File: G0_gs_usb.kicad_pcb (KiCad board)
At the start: 2 copper layers, 25.9 x 53.3 mm, 59 parts, among them J1 USB_C_Receptacle_USB2.0, J2 CAN1, J3 CAN2, J4 Conn_01x03_Pin, SW1 SW_Push_Dual, U1 STM32G0B1CBTx, U2 TJA1042T-3, U3 TJA1042T-3, U4 XC6206PxxxMR

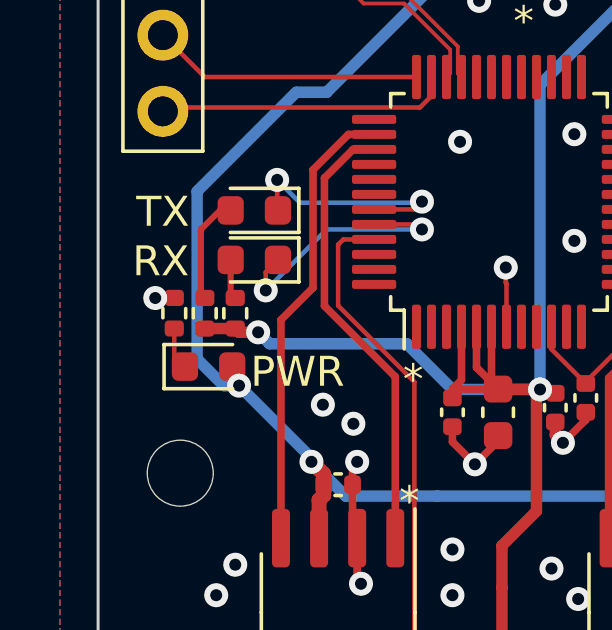
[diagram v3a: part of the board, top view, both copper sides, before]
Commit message: Update net labels to match the purpose of the pins.
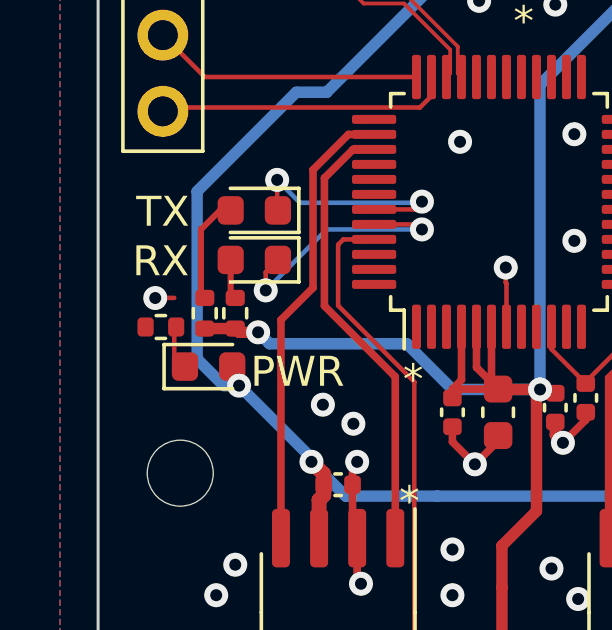
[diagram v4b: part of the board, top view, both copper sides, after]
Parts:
- R10, R11, R12, R13: value 22 -> 1k
- R14: value 1k -> 5.1k
- moved R14 0.64 mm to (54.2, 88.3), turned to 0 degrees
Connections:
- R14 pad 1: Net-(D8-K) -> GND
- R14 pad 2: GND -> Net-(D8-K)
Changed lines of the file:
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@@
+    )
+  )
+  (footprint "Resistor_SMD:R_0402_1005Metric" (layer "F.Cu")
+    (at 54.162939 88.342353)
+    (descr "Resistor SMD 0402 (1005 Metric), square (rectangular) end terminal, IPC_7351 nominal, (Body size source: IPC-SM-782 page 72, https://www.pcb-3d.com/wordpress/wp-content/uploads/ipc-sm-782a_amendment_1_and_2.pdf), generated with kicad-footprint-generator")
+    (tags "resistor")
+    (property "LCSC Part #" "C11616")
+    (property "Part #" "0402WGF5103TCE")
+    (property "Sheetfile" "G0_gs_usb.kicad_sch")
+    (property "Sheetname" "")
+    (property "ki_description" "Resistor")
+    (property "ki_keywords" "R res resistor")
+    (attr smd)
+    (fp_text reference "R14" (at 0 -1.17) (layer "F.SilkS") hide
+        (effects (font (size 1 1) (thickness 0.15)))
+    )
+    (fp_text value "5.1k" (at 0 1.17) (layer "F.Fab")
+        (effects (font (size 1 1) (thickness 0.15)))
+    )
+    (fp_text user "${REFERENCE}" (at 0 0) (layer "F.Fab")
+        (effects (font (size 0.26 0.26) (thickness 0.04)))
+    )
+    (fp_line (start -0.153641 -0.38) (end 0.153641 -0.38)
+      (stroke (width 0.12) (type solid)) (layer "F.SilkS"))
+    (fp_line (start -0.153641 0.38) (end 0.153641 0.38)
+      (stroke (width 0.12) (type solid)) (layer "F.SilkS"))
+    (fp_line (start -0.93 -0.47) (end 0.93 -0.47)
+      (stroke (width 0.05) (type solid)) (layer "F.CrtYd"))
+    (fp_line (start -0.93 0.47) (end -0.93 -0.47)
+      (stroke (width 0.05) (type solid)) (layer "F.CrtYd"))
+    (fp_line (start 0.93 -0.47) (end 0.93 0.47)
+      (stroke (width 0.05) (type solid)) (layer "F.CrtYd"))
+    (fp_line (start 0.93 0.47) (end -0.93 0.47)
+      (stroke (width 0.05) (type solid)) (layer "F.CrtYd"))
+    (fp_line (start -0.525 -0.27) (end 0.525 -0.27)
+      (stroke (width 0.1) (type solid)) (layer "F.Fab"))
+    (fp_line (start -0.525 0.27) (end -0.525 -0.27)
+      (stroke (width 0.1) (type solid)) (layer "F.Fab"))
+    (fp_line (start 0.525 -0.27) (end 0.525 0.27)
+      (stroke (width 0.1) (type solid)) (layer "F.Fab"))
+    (fp_line (start 0.525 0.27) (end -0.525 0.27)
+      (stroke (width 0.1) (type solid)) (layer "F.Fab"))
+    (pad "1" smd roundrect (at -0.51 0) (size 0.54 0.64) (layers "F.Cu" "F.Paste" "F.Mask") (roundrect_rratio 0.25)
+      (net 2 "GND") (pintype "passive"))
+    (pad "2" smd roundrect (at 0.51 0) (size 0.54 0.64) (layers "F.Cu" "F.Paste" "F.Mask") (roundrect_rratio 0.25)
+      (net 9 "Net-(D8-K)") (pintype "passive"))
+    (model "${KICAD6_3DMODEL_DIR}/Resistor_SMD.3dshapes/R_0402_1005Metric.wrl"
+      (offset (xyz 0 0 0))
+      (scale (xyz 1 1 1))
+      (rotate (xyz 0 0 0))
     )
   )
@@
     (descr "Resistor SMD 0402 (1005 Metric), square (rectangular) end terminal, IPC_7351 nominal, (Body size source: IPC-SM-782 page 72, https://www.pcb-3d.com/wordpress/wp-content/uploads/ipc-sm-782a_amendment_1_and_2.pdf), generated with kicad-footprint-generator")
     (tags "resistor")
-    (property "LCSC Part #" "C25092")
-    (property "Part #" "0402WGF220JTCE")
+    (property "LCSC Part #" "C11702")
+    (property "Part #" "0402WGF1001TCE")
     (property "Sheetfile" "G0_gs_usb.kicad_sch")
     (property "Sheetname" "")
@@
         (effects (font (size 1 1) (thickness 0.15)))
     )
-    (fp_text value "22" (at 0 1.17 -90) (layer "F.Fab")
+    (fp_text value "1k" (at 0 1.17 -90) (layer "F.Fab")
         (effects (font (size 1 1) (thickness 0.15)))
     )
@@
       (net 4 "/5V") (pinfunction "A") (pintype "passive"))
     (model "${KICAD6_3DMODEL_DIR}/LED_SMD.3dshapes/LED_0603_1608Metric.wrl"
-      (offset (xyz 0 0 0))
-      (scale (xyz 1 1 1))
-      (rotate (xyz 0 0 0))
-    )
-  )
-  (footprint "Resistor_SMD:R_0402_1005Metric" (layer "F.Cu")
-    (at 54.61 87.882 90)
-    (descr "Resistor SMD 0402 (1005 Metric), square (rectangular) end terminal, IPC_7351 nominal, (Body size source: IPC-SM-782 page 72, https://www.pcb-3d.com/wordpress/wp-content/uploads/ipc-sm-782a_amendment_1_and_2.pdf), generated with kicad-footprint-generator")
-    (tags "resistor")
-    (property "LCSC Part #" "C11702")
-    (property "Part #" "0402WGF1001TCE")
-    (property "Sheetfile" "G0_gs_usb.kicad_sch")
-    (property "Sheetname" "")
-    (property "ki_description" "Resistor")
-    (property "ki_keywords" "R res resistor")
-    (attr smd)
-    (fp_text reference "R14" (at 0 -1.17 90) (layer "F.SilkS") hide
-        (effects (font (size 1 1) (thickness 0.15)))
-    )
-    (fp_text value "1k" (at 0 1.17 90) (layer "F.Fab")
-        (effects (font (size 1 1) (thickness 0.15)))
-    )
-    (fp_text user "${REFERENCE}" (at 0 0 90) (layer "F.Fab")
-        (effects (font (size 0.26 0.26) (thickness 0.04)))
-    )
-    (fp_line (start -0.153641 -0.38) (end 0.153641 -0.38)
-      (stroke (width 0.12) (type solid)) (layer "F.SilkS"))
-    (fp_line (start -0.153641 0.38) (end 0.153641 0.38)
-      (stroke (width 0.12) (type solid)) (layer "F.SilkS"))
-    (fp_line (start -0.93 -0.47) (end 0.93 -0.47)
-      (stroke (width 0.05) (type solid)) (layer "F.CrtYd"))
-    (fp_line (start -0.93 0.47) (end -0.93 -0.47)
-      (stroke (width 0.05) (type solid)) (layer "F.CrtYd"))
-    (fp_line (start 0.93 -0.47) (end 0.93 0.47)
-      (stroke (width 0.05) (type solid)) (layer "F.CrtYd"))
-    (fp_line (start 0.93 0.47) (end -0.93 0.47)
-      (stroke (width 0.05) (type solid)) (layer "F.CrtYd"))
-    (fp_line (start -0.525 -0.27) (end 0.525 -0.27)
-      (stroke (width 0.1) (type solid)) (layer "F.Fab"))
-    (fp_line (start -0.525 0.27) (end -0.525 -0.27)
-      (stroke (width 0.1) (type solid)) (layer "F.Fab"))
-    (fp_line (start 0.525 -0.27) (end 0.525 0.27)
-      (stroke (width 0.1) (type solid)) (layer "F.Fab"))
-    (fp_line (start 0.525 0.27) (end -0.525 0.27)
-      (stroke (width 0.1) (type solid)) (layer "F.Fab"))
-    (pad "1" smd roundrect (at -0.51 0 90) (size 0.54 0.64) (layers "F.Cu" "F.Paste" "F.Mask") (roundrect_rratio 0.25)
-      (net 9 "Net-(D8-K)") (pintype "passive"))
-    (pad "2" smd roundrect (at 0.51 0 90) (size 0.54 0.64) (layers "F.Cu" "F.Paste" "F.Mask") (roundrect_rratio 0.25)
-      (net 2 "GND") (pintype "passive"))
-    (model "${KICAD6_3DMODEL_DIR}/Resistor_SMD.3dshapes/R_0402_1005Metric.wrl"
       (offset (xyz 0 0 0))
       (scale (xyz 1 1 1))
@@
     (descr "Resistor SMD 0402 (1005 Metric), square (rectangular) end terminal, IPC_7351 nominal, (Body size source: IPC-SM-782 page 72, https://www.pcb-3d.com/wordpress/wp-content/uploads/ipc-sm-782a_amendment_1_and_2.pdf), generated with kicad-footprint-generator")
     (tags "resistor")
-    (property "LCSC Part #" "C25092")
-    (property "Part #" "0402WGF220JTCE")
+    (property "LCSC Part #" "C11702")
+    (property "Part #" "0402WGF1001TCE")
     (property "Sheetfile" "G0_gs_usb.kicad_sch")
     (property "Sheetname" "")
@@
         (effects (font (size 1 1) (thickness 0.15)))
     )
-    (fp_text value "22" (at 0 1.17 90) (layer "F.Fab")
+    (fp_text value "1k" (at 0 1.17 90) (layer "F.Fab")
         (effects (font (size 1 1) (thickness 0.15)))
     )
@@
     (descr "Resistor SMD 0402 (1005 Metric), square (rectangular) end terminal, IPC_7351 nominal, (Body size source: IPC-SM-782 page 72, https://www.pcb-3d.com/wordpress/wp-content/uploads/ipc-sm-782a_amendment_1_and_2.pdf), generated with kicad-footprint-generator")
     (tags "resistor")
-    (property "LCSC Part #" "C25092")
-    (property "Part #" "0402WGF220JTCE")
+    (property "LCSC Part #" "C11702")
+    (property "Part #" "0402WGF1001TCE")
     (property "Sheetfile" "G0_gs_usb.kicad_sch")
     (property "Sheetname" "")
@@
         (effects (font (size 1 1) (thickness 0.15)))
     )
-    (fp_text value "22" (at 0 1.17 -90) (layer "F.Fab")
+    (fp_text value "1k" (at 0 1.17 -90) (layer "F.Fab")
         (effects (font (size 1 1) (thickness 0.15)))
     )
@@
     (descr "Resistor SMD 0402 (1005 Metric), square (rectangular) end terminal, IPC_7351 nominal, (Body size source: IPC-SM-782 page 72, https://www.pcb-3d.com/wordpress/wp-content/uploads/ipc-sm-782a_amendment_1_and_2.pdf), generated with kicad-footprint-generator")
     (tags "resistor")
-    (property "LCSC Part #" "C25092")
-    (property "Part #" "0402WGF220JTCE")
+    (property "LCSC Part #" "C11702")
+    (property "Part #" "0402WGF1001TCE")
     (property "Sheetfile" "G0_gs_usb.kicad_sch")
     (property "Sheetname" "")
@@
         (effects (font (size 1 1) (thickness 0.15)))
     )
-    (fp_text value "22" (at 0 1.17 90) (layer "F.Fab")
-        (effects (font (size 1 1) (thickness 0.15)))
-    )
+    (fp_text value "1k" (at 0 1.17 90) (layer "F.Fab")
+        (effects (font (size 1 1) (thickness 0.15)))
+    )
